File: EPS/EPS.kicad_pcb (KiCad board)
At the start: 2 copper layers, 50 parts, among them IC1 TPS63802DLAT, IC2 TPS63802DLAT, IC3 TPS63802DLAT, IC4 TPS63802DLAT, IC5 TPS63802DLAT, IC6 TPS63802DLAT

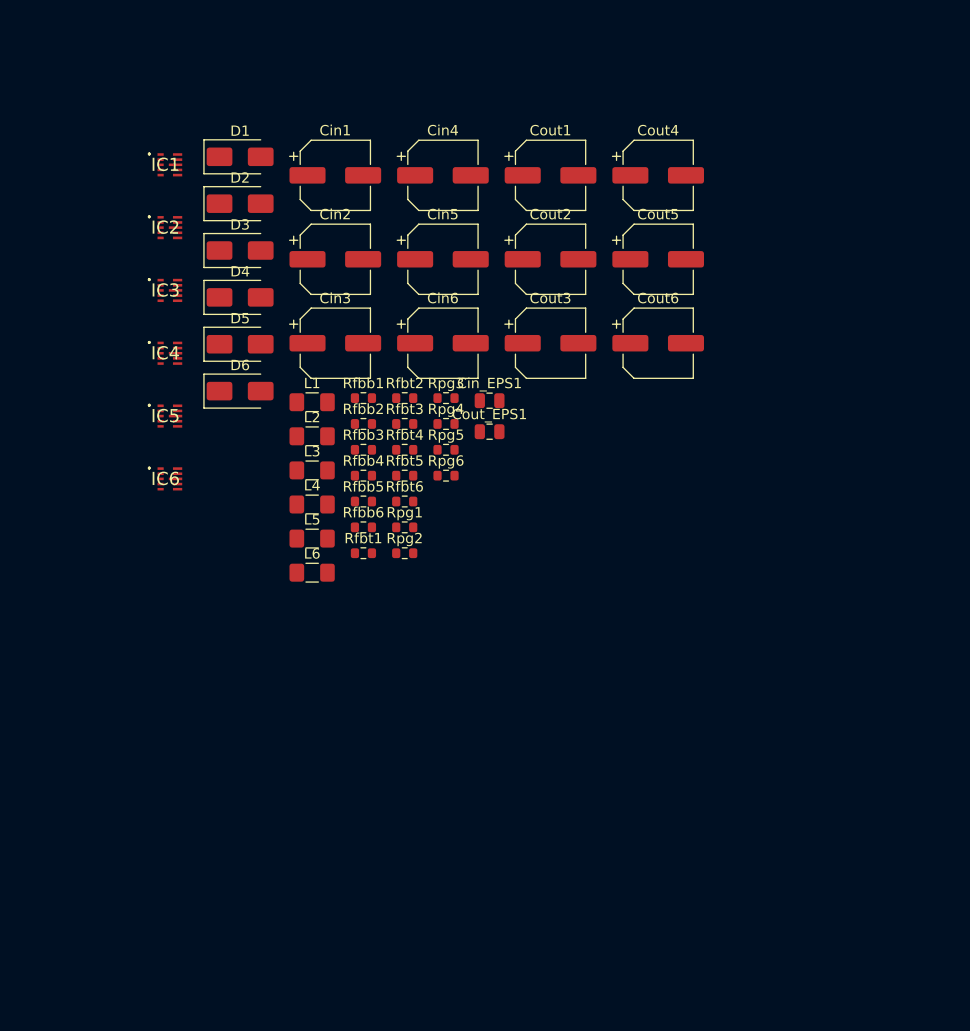
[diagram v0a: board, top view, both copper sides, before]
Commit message: Add files via upload
Al sistema EPS se le añadió el micro, y el componente encargado de la proteccion, hay que modificar las uniones todavia, y a ser posible añadir sensores para medir lo que nos interesa
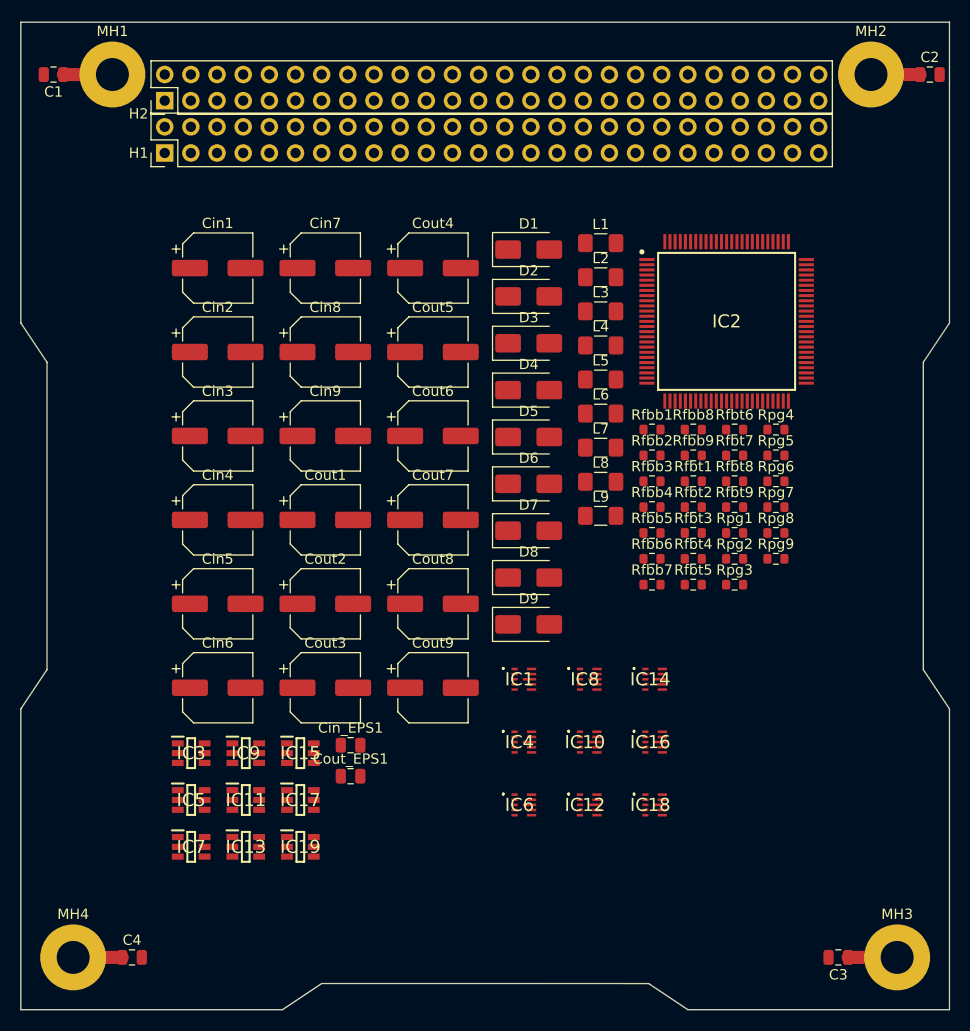
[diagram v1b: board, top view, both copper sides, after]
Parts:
- added C1: 0.1uF, Capacitor_SMD:C_0805_2012Metric, F.Cu at (104.8, 55.9)
- added C2: 0.1uF, Capacitor_SMD:C_0805_2012Metric, F.Cu at (189.9, 55.9)
- added C3: 0.1uF, Capacitor_SMD:C_0805_2012Metric, F.Cu at (181.0, 141.6)
- added C4: 0.1uF, Capacitor_SMD:C_0805_2012Metric, F.Cu at (112.4, 141.6)
- added Cin7: 22uF, Capacitor_SMD:CP_Elec_6.3x4.5, F.Cu at (131.2, 74.7)
- added Cin8: 22uF, Capacitor_SMD:CP_Elec_6.3x4.5, F.Cu at (131.2, 82.8)
- added Cin9: 22uF, Capacitor_SMD:CP_Elec_6.3x4.5, F.Cu at (131.2, 91.0)
- added Cout7: 22uF, Capacitor_SMD:CP_Elec_6.3x4.5, F.Cu at (141.6, 99.1)
- added Cout8: 22uF, Capacitor_SMD:CP_Elec_6.3x4.5, F.Cu at (141.6, 107.3)
- added Cout9: 22uF, Capacitor_SMD:CP_Elec_6.3x4.5, F.Cu at (141.6, 115.4)
- added D7: SS14, Diode_SMD:D_SMA, F.Cu at (150.9, 100.2)
- added D8: SS14, Diode_SMD:D_SMA, F.Cu at (150.9, 104.7)
- added D9: SS14, Diode_SMD:D_SMA, F.Cu at (150.9, 109.3)
- added H1: Stack Header, Connector_PinHeader_2.54mm:PinHeader_2x26_P2.54mm_Vertical, F.Cu at (115.6, 63.5)
- added H2: Stack Header, Connector_PinHeader_2.54mm:PinHeader_2x26_P2.54mm_Vertical, F.Cu at (115.6, 58.4)
- added IC10: TPS63802DLAT, SamacSys_Parts:TPS63802DLAT, F.Cu at (156.8, 120.7)
- added IC11: MP62551DJ-LF-Z, micro:SOT95P280X100-6N, F.Cu at (123.4, 126.3)
- added IC12: TPS63802DLAT, SamacSys_Parts:TPS63802DLAT, F.Cu at (156.8, 126.8)
- added IC13: MP62551DJ-LF-Z, micro:SOT95P280X100-6N, F.Cu at (123.4, 130.9)
- added IC14: TPS63802DLAT, SamacSys_Parts:TPS63802DLAT, F.Cu at (163.1, 114.6)
- added IC15: MP62551DJ-LF-Z, micro:SOT95P280X100-6N, F.Cu at (128.7, 121.8)
- added IC16: TPS63802DLAT, SamacSys_Parts:TPS63802DLAT, F.Cu at (163.1, 120.7)
- added IC17: MP62551DJ-LF-Z, micro:SOT95P280X100-6N, F.Cu at (128.7, 126.3)
- added IC18: TPS63802DLAT, SamacSys_Parts:TPS63802DLAT, F.Cu at (163.1, 126.8)
- added IC19: MP62551DJ-LF-Z, micro:SOT95P280X100-6N, F.Cu at (128.7, 130.9)
- added IC7: MP62551DJ-LF-Z, micro:SOT95P280X100-6N, F.Cu at (118.1, 130.9)
- added IC8: TPS63802DLAT, SamacSys_Parts:TPS63802DLAT, F.Cu at (156.8, 114.6)
- added IC9: MP62551DJ-LF-Z, micro:SOT95P280X100-6N, F.Cu at (123.4, 121.8)
- added L7: 470nH, Inductor_SMD:L_1206_3216Metric_Pad1.42x1.75mm_HandSolder, F.Cu at (157.9, 92.1)
- added L8: 470nH, Inductor_SMD:L_1206_3216Metric_Pad1.42x1.75mm_HandSolder, F.Cu at (157.9, 95.4)
- added L9: 470nH, Inductor_SMD:L_1206_3216Metric_Pad1.42x1.75mm_HandSolder, F.Cu at (157.9, 98.7)
- added MH1: M3, MountingHole:MountingHole_3.2mm_M3_Pad, F.Cu at (110.5, 55.9)
- added MH2: M3, MountingHole:MountingHole_3.2mm_M3_Pad, F.Cu at (184.2, 55.9)
- added MH3: M3, MountingHole:MountingHole_3.2mm_M3_Pad, F.Cu at (186.7, 141.6)
- added MH4: M3, MountingHole:MountingHole_3.2mm_M3_Pad, F.Cu at (106.7, 141.6)
- added Rfbb7: 91000, Resistor_SMD:R_0603_1608Metric, F.Cu at (162.9, 105.4)
- added Rfbb8: 91000, Resistor_SMD:R_0603_1608Metric, F.Cu at (166.9, 90.4)
- added Rfbb9: 91000, Resistor_SMD:R_0603_1608Metric, F.Cu at (166.9, 92.9)
- added Rfbt7: 511000, Resistor_SMD:R_0603_1608Metric, F.Cu at (170.9, 92.9)
- added Rfbt8: 511000, Resistor_SMD:R_0603_1608Metric, F.Cu at (170.9, 95.4)
- added Rfbt9: 511000, Resistor_SMD:R_0603_1608Metric, F.Cu at (170.9, 97.9)
- added Rpg7: 100000, Resistor_SMD:R_0603_1608Metric, F.Cu at (174.9, 97.9)
- added Rpg8: 100000, Resistor_SMD:R_0603_1608Metric, F.Cu at (174.9, 100.4)
- added Rpg9: 100000, Resistor_SMD:R_0603_1608Metric, F.Cu at (174.9, 102.9)
- IC2: value TPS63802DLAT -> STM32G474VET6; footprint SamacSys_Parts:TPS63802DLAT -> micro:QFP50P1600X1600X160-100N
- IC3, IC5: value TPS63802DLAT -> MP62551DJ-LF-Z; footprint SamacSys_Parts:TPS63802DLAT -> micro:SOT95P280X100-6N
- moved IC1 60.6 mm to (150.4, 114.6)
- moved IC2 54.8 mm to (170.1, 79.9)
- moved IC4 51.1 mm to (150.4, 120.7)
- moved IC6 46.7 mm to (150.4, 126.8)
- moved IC3 45.0 mm to (118.1, 121.8)
- moved Cin4 40.0 mm to (120.7, 99.1)
- moved Cin6 40.0 mm to (120.7, 115.4)
- moved Cout1 40.0 mm to (131.2, 99.1)
- moved Cout3 40.0 mm to (131.2, 115.4)
- moved Cin5 40.0 mm to (120.7, 107.3)
- moved Cout2 40.0 mm to (131.2, 107.3)
- moved IC5 37.3 mm to (118.1, 126.3)
- moved Cout_EPS1 36.1 mm to (133.6, 124.0)
- moved Cin_EPS1 36.1 mm to (133.6, 121.0)
- moved Rpg3 33.4 mm to (170.9, 105.4)
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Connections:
- Cout2 pad 1: Net-(D3-A) -> Net-(D1-A)
- Cout3 pad 1: Net-(D4-A) -> Net-(D3-A)
- Cout4 pad 1: Net-(D5-A) -> Net-(D4-A)
- Cout5 pad 1: Net-(D1-A) -> Net-(D5-A)
- D1 pad 1: Vout_EPS -> Net-(D1-K)
- D2 pad 1: Vout_EPS -> Net-(D2-K)
- D3 pad 1: Vout_EPS -> Net-(D3-K)
- D4 pad 1: Vout_EPS -> Net-(D4-K)
- D5 pad 1: Vout_EPS -> Net-(D5-K)
- D6 pad 1: Vout_EPS -> Net-(D6-K)
- IC2 pad 1: Vin_EPS -> unconnected-(IC2-PE2-Pad1)
- IC2 pad 10: Vin_EPS -> unconnected-(IC2-PF9-Pad10)
- IC2 pad 2: GND -> unconnected-(IC2-PE3-Pad2)
- IC2 pad 3: GND -> unconnected-(IC2-PE4-Pad3)
- IC2 pad 4: Net-(IC2-FB) -> unconnected-(IC2-PE5-Pad4)
- IC2 pad 5: Net-(IC2-PG) -> unconnected-(IC2-PE6-Pad5)
- IC2 pad 6: Net-(D3-A) -> unconnected-(IC2-VBAT-Pad6)
- IC2 pad 7: Net-(IC2-L2) -> unconnected-(IC2-PC13-Pad7)
- IC2 pad 8: GND -> unconnected-(IC2-PC14-OSC32_IN-Pad8)
- IC2 pad 9: Net-(IC2-L1) -> unconnected-(IC2-PC15-OSC32_OUT-Pad9)
- IC3 pad 1: Vin_EPS -> Net-(D2-K)
- IC3 pad 3: GND -> /EN_0
- IC3 pad 4: Net-(IC3-FB) -> /FLAG_0
- IC3 pad 5: Net-(IC3-PG) -> unconnected-(IC3-ILIM-Pad5)
- IC3 pad 6: Net-(D4-A) -> Vout_EPS
- IC4 pad 6: Net-(D5-A) -> Net-(D1-A)
- IC5 pad 1: Vin_EPS -> Net-(D1-K)
- IC5 pad 3: GND -> /EN_1
- IC5 pad 4: Net-(IC5-FB) -> /FLAG_1
- IC5 pad 5: Net-(IC5-PG) -> unconnected-(IC5-ILIM-Pad5)
- IC5 pad 6: Net-(D1-A) -> Vout_EPS
- IC6 pad 6: Net-(D6-A) -> Net-(D3-A)
- L2 pad 1: Net-(IC2-L2) -> Net-(IC4-L2)
- L2 pad 2: Net-(IC2-L1) -> Net-(IC4-L1)
- L3 pad 1: Net-(IC3-L2) -> Net-(IC6-L2)
- L3 pad 2: Net-(IC3-L1) -> Net-(IC6-L1)
- L4 pad 1: Net-(IC4-L2) -> Net-(IC8-L2)
- L4 pad 2: Net-(IC4-L1) -> Net-(IC8-L1)
- L5 pad 1: Net-(IC5-L2) -> Net-(IC10-L2)
- L5 pad 2: Net-(IC5-L1) -> Net-(IC10-L1)
- L6 pad 1: Net-(IC6-L2) -> Net-(IC12-L2)
- L6 pad 2: Net-(IC6-L1) -> Net-(IC12-L1)
- Rfbb2 pad 1: Net-(IC2-FB) -> Net-(IC4-FB)
- Rfbb3 pad 1: Net-(IC3-FB) -> Net-(IC6-FB)
- Rfbb4 pad 1: Net-(IC4-FB) -> Net-(IC8-FB)
- Rfbb5 pad 1: Net-(IC5-FB) -> Net-(IC10-FB)
- Rfbb6 pad 1: Net-(IC6-FB) -> Net-(IC12-FB)
- Rfbt2 pad 1: Net-(D3-A) -> Net-(D1-A)
- Rfbt2 pad 2: Net-(IC2-FB) -> Net-(IC4-FB)
- Rfbt3 pad 1: Net-(D4-A) -> Net-(D3-A)
- Rfbt3 pad 2: Net-(IC3-FB) -> Net-(IC6-FB)
- Rfbt4 pad 1: Net-(D5-A) -> Net-(D4-A)
- Rfbt4 pad 2: Net-(IC4-FB) -> Net-(IC8-FB)
- Rfbt5 pad 1: Net-(D1-A) -> Net-(D5-A)
- Rfbt5 pad 2: Net-(IC5-FB) -> Net-(IC10-FB)
- Rfbt6 pad 2: Net-(IC6-FB) -> Net-(IC12-FB)
- Rpg2 pad 1: Net-(D3-A) -> Net-(D1-A)
- Rpg2 pad 2: Net-(IC2-PG) -> Net-(IC4-PG)
- Rpg3 pad 1: Net-(D4-A) -> Net-(D3-A)
- Rpg3 pad 2: Net-(IC3-PG) -> Net-(IC6-PG)
- Rpg4 pad 1: Net-(D5-A) -> Net-(D4-A)
- Rpg4 pad 2: Net-(IC4-PG) -> Net-(IC8-PG)
- Rpg5 pad 1: Net-(D1-A) -> Net-(D5-A)
- Rpg5 pad 2: Net-(IC5-PG) -> Net-(IC10-PG)
- Rpg6 pad 2: Net-(IC6-PG) -> Net-(IC12-PG)
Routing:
- net Net-(C1-Pad1): track 0.00 -> 4.77 mm
- net Net-(C2-Pad1): track 0.00 -> 4.77 mm
- net Net-(C4-Pad1): track 0.00 -> 4.76 mm
- net Net-(C3-Pad1): track 0.00 -> 4.76 mm
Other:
- board outline added: 90.2 x 95.9 mm
